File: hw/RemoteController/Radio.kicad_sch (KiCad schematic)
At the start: 89 parts, among them J4 BWSMA-KWE-Z3.5*4.2, U1 LM358, U10 H3-TCD-12-222X+, U12 MAX1473EUI+, U16 H3-TCD-12-222X+, U17 AD8313xRM, U18 LM358, U3 SPF5043Z, U5 XA17-G4K, U6 MAX7044AKA, U8 AD8313xRM, U9 GVA-63, Y2 6.6128 MHz, Y3 10.7 MHz, Y4 13.56 MHz

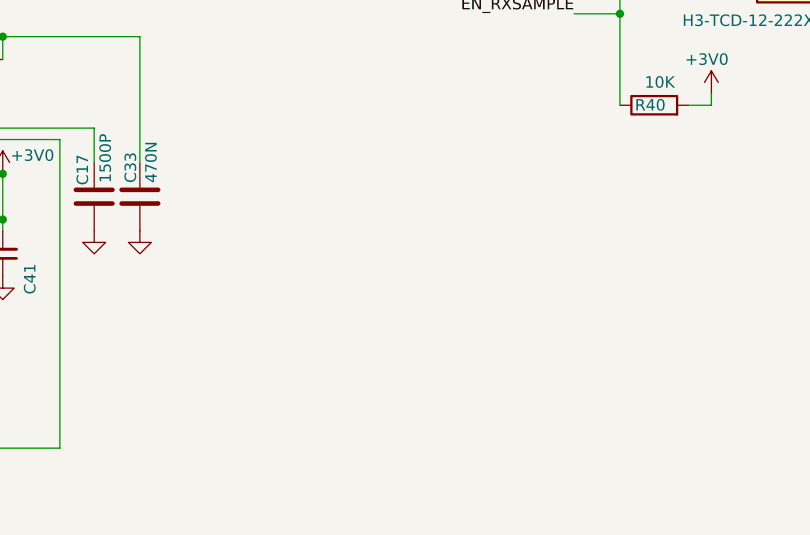
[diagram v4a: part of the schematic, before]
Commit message: remote_ctrl: half way to placement, replace max1473 wit, micrf220
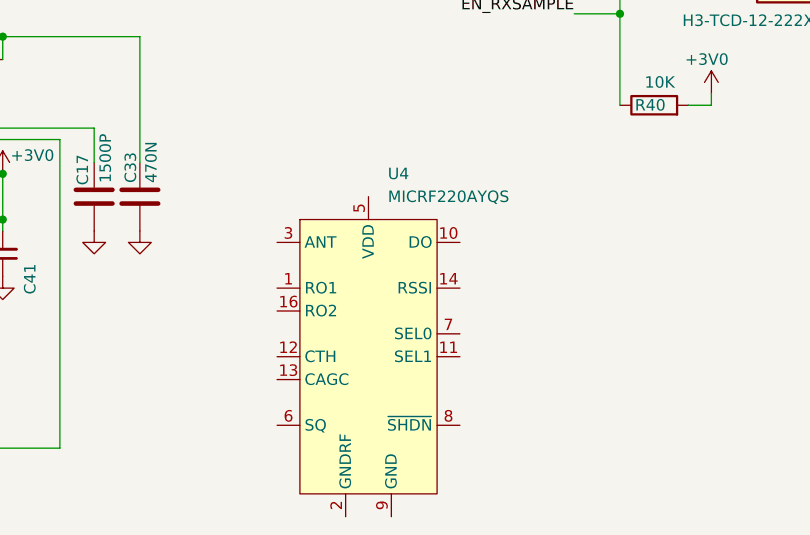
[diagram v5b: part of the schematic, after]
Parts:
- added U4: MICRF220AYQS, Package_SO:QSOP-16_3.9x4.9mm_P0.635mm, symbol RF:MICRF220AYQS
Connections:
- net at U16.4 (OUT): now also C29.2
- new net: U4.2 (GNDRF), U4.4 (GNDRF)
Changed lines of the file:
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@@
+	)
+	(symbol
+		(lib_id "RF:MICRF220AYQS")
+		(at 133.35 177.8 0)
+		(unit 1)
+		(body_style 1)
+		(exclude_from_sim no)
+		(in_bom yes)
+		(on_board yes)
+		(in_pos_files yes)
+		(dnp no)
+		(fields_autoplaced yes)
+		(property "Reference" "U4"
+			(at 135.4933 157.48 0)
+			(show_name no)
+			(do_not_autoplace no)
+			(effects
+				(font
+					(size 1.27 1.27)
+				)
+				(justify left)
+			)
+		)
+		(property "Value" "MICRF220AYQS"
+			(at 135.4933 160.02 0)
+			(show_name no)
+			(do_not_autoplace no)
+			(effects
+				(font
+					(size 1.27 1.27)
+				)
+				(justify left)
+			)
+		)
+		(property "Footprint" "Package_SO:QSOP-16_3.9x4.9mm_P0.635mm"
+			(at 133.35 198.12 0)
+			(hide yes)
+			(show_name no)
+			(do_not_autoplace no)
+			(effects
+				(font
+					(size 1.27 1.27)
+				)
+			)
+		)
+		(property "Datasheet" "http://ww1.microchip.com/downloads/en/DeviceDoc/micrf220.pdf"
+			(at 142.24 158.75 0)
+			(hide yes)
+			(show_name no)
+			(do_not_autoplace no)
+			(effects
+				(font
+					(size 1.27 1.27)
+				)
+			)
+		)
+		(property "Description" "ASK Receiver 3.0-3.6V, 300-450MHz, -110dBm, QSOP-16"
+			(at 133.35 177.8 0)
+			(hide yes)
+			(show_name no)
+			(do_not_autoplace no)
+			(effects
+				(font
+					(size 1.27 1.27)
+				)
+			)
+		)
+		(pin "8"
+		)
+		(pin "6"
+		)
+		(pin "14"
+		)
+		(pin "5"
+		)
+		(pin "1"
+		)
+		(pin "7"
+		)
+		(pin "2"
+		)
+		(pin "12"
+		)
+		(pin "13"
+		)
+		(pin "4"
+		)
+		(pin "3"
+		)
+		(pin "16"
+		)
+		(pin "15"
+		)
+		(pin "9"
+		)
+		(pin "10"
+		)
+		(pin "11"
+		)
+		(instances
+			(project "RemoteController"
+				(path "/2496396e-da71-4b2e-9ac4-452e5130442d/d59aad70-30f5-48a2-8092-bdb11e43ed29"
+					(reference "U4")
+					(unit 1)
+				)
+			)
+		)
 	)
 	(symbol

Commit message: remote_ctrl: continue placemen
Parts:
- removed C25: 470P, Capacitor_SMD:C_0402_1005Metric_Pad0.74x0.62mm_HandSolder, symbol Device:C_Small
- removed C28, C29, C49: 100P, Capacitor_SMD:C_0402_1005Metric_Pad0.74x0.62mm_HandSolder, symbol Device:C_Small
- removed C33: 470N, Capacitor_SMD:C_0402_1005Metric_Pad0.74x0.62mm_HandSolder, symbol Device:C
- removed C40: 10N, Capacitor_SMD:C_0402_1005Metric_Pad0.74x0.62mm_HandSolder, symbol Device:C_Small
- removed C41: 220P, Capacitor_SMD:C_0402_1005Metric_Pad0.74x0.62mm_HandSolder, symbol Device:C_Small
- removed C42: 220P, Capacitor_SMD:C_0402_1005Metric_Pad0.74x0.62mm_HandSolder, symbol Device:C
- removed C50: 2P7, Capacitor_SMD:C_0402_1005Metric_Pad0.74x0.62mm_HandSolder, symbol Device:C_Small
- removed L5: 56N, Inductor_SMD:L_0603_1608Metric_Pad1.05x0.95mm_HandSolder, symbol Device:L
- removed L6, L7: 15N, Inductor_SMD:L_0603_1608Metric_Pad1.05x0.95mm_HandSolder, symbol Device:L
- removed R20: 5K1, Resistor_SMD:R_0402_1005Metric_Pad0.72x0.64mm_HandSolder, symbol Device:R
- removed R21, R22, R23, R24: 0R, Resistor_SMD:R_0402_1005Metric_Pad0.72x0.64mm_HandSolder, symbol Device:R
- removed U12: MAX1473EUI+, Package_SO:TSSOP-28_4.4x9.7mm_P0.65mm, symbol steew:MAX1473EUI+
- removed Y2: 6.6128 MHz, Crystal:Crystal_SMD_HC49-SD, symbol Device:Crystal
- removed Y3: 10.7 MHz, Crystal:Resonator_SMD_Murata_SFECV-3Pin_6.9x2.9mm_HandSoldering, symbol Device:Resonator
- added C25: 10P, Capacitor_SMD:C_0402_1005Metric_Pad0.74x0.62mm_HandSolder, symbol Device:C
- added C33: 100N, Capacitor_SMD:C_0402_1005Metric_Pad0.74x0.62mm_HandSolder, symbol Device:C_Small
- added L5: VHF160808H39NJT, Inductor_SMD:L_0603_1608Metric_Pad1.05x0.95mm_HandSolder, symbol Device:L_Ferrite_Small
- added R41: 100R, Resistor_SMD:R_0402_1005Metric_Pad0.72x0.64mm_HandSolder, symbol Device:R
- added Y2: L327S13CU11L, Crystal:Crystal_SMD_3225-4Pin_3.2x2.5mm_HandSoldering, symbol Device:Crystal_GND24_Small
- C1, C2: value C -> 10P
- C17: value 1500P -> 10P; KiLib_Generator (none) -> SMD_2terminal_chip_molded
- C35: value 10N -> 1000P; KiLib_Generator (none) -> SMD_2terminal_chip_molded
- C38: value 10N -> 100N; KiLib_Generator (none) -> SMD_2terminal_chip_molded
- C39: value 100N -> 4U7
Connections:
- net +3V0: now also C38.1, U4.5 (VDD); no longer C35.2, C38.2, C39.2
- net DATAOUT: now also U4.10 (DO)
- net GND: now also C17.1, C38.2, C39.2, U4.2 (GNDRF), U4.4 (GNDRF), U4.9 (GND), C25.1, C33.2, L5.1, Y2.2 (G), Y2.4 (G); no longer C17.2, C35.1, C38.1, C39.1
- net at U16.4 (OUT): now also C35.2
- net at U4.1 (RO1): now also C25.2, Y2.3
- net RX_BW_SEL1: now reaches U4.11 (SEL1)
- net at U4.12 (CTH): now also C33.1
- net at U4.13 (CAGC): now also C39.1
- net RX_RSSI: now reaches U4.14 (RSSI)
- net at U4.16 (RO2): now also C17.2, Y2.1
- net at U4.3 (ANT): now also C35.1, L5.2
- net RX_SQUELCH: now reaches U4.6 (SQ)
- net RX_BW_SEL0: now reaches U4.7 (SEL0)
- net at U4.8 (~{SHDN}): now also R41.2
- net RXEN renamed RF_SEL0
- net ~{TXEN} renamed RF_SEL1
- new net ~{RX_SHDN}: R41.1
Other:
- note added: "RECEIVER"
- moved on the sheet: U4

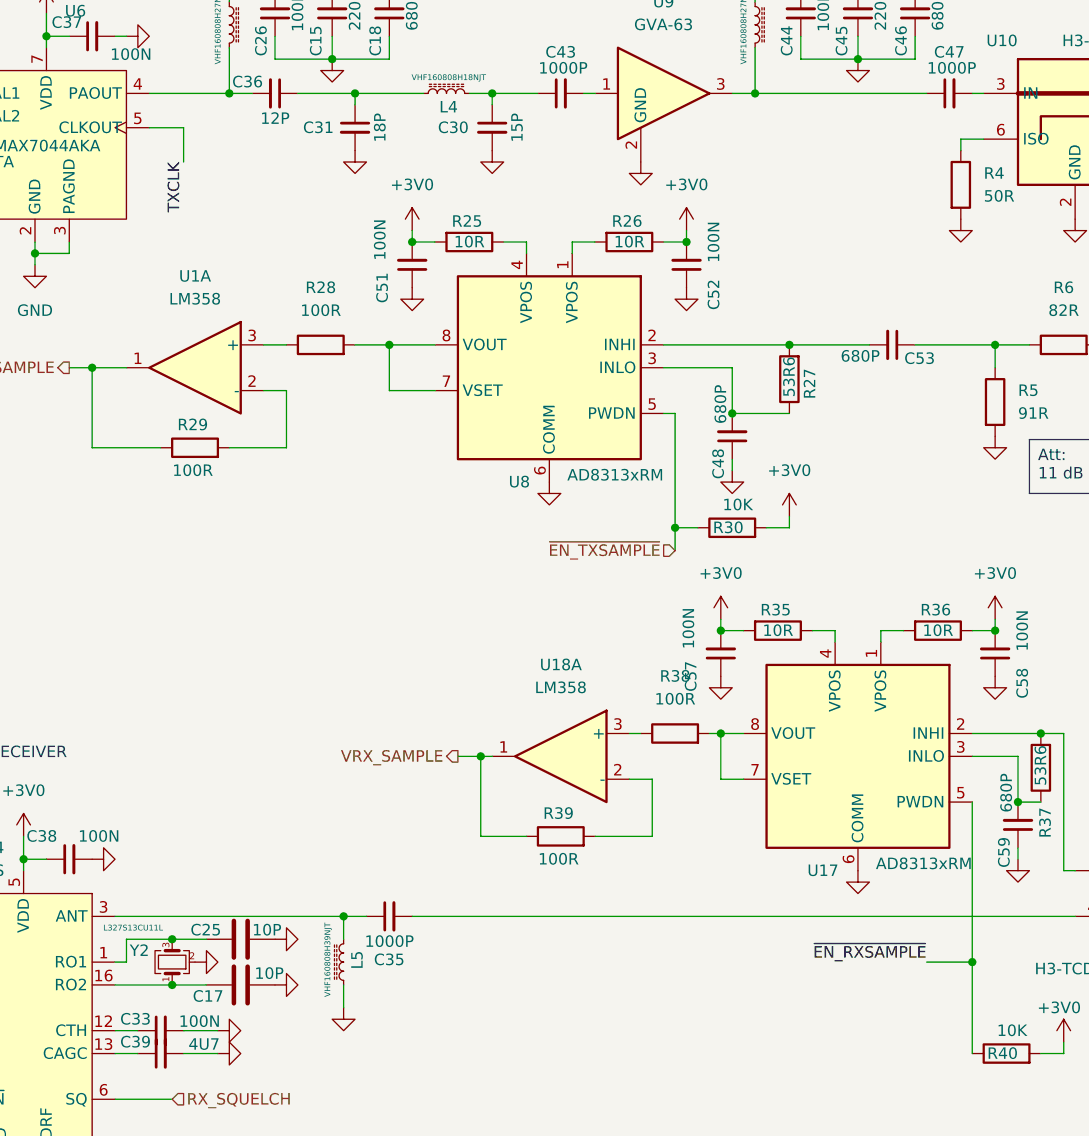
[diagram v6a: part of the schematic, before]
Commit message: remote_ctrl: fix some schematic issues, add battery PTC
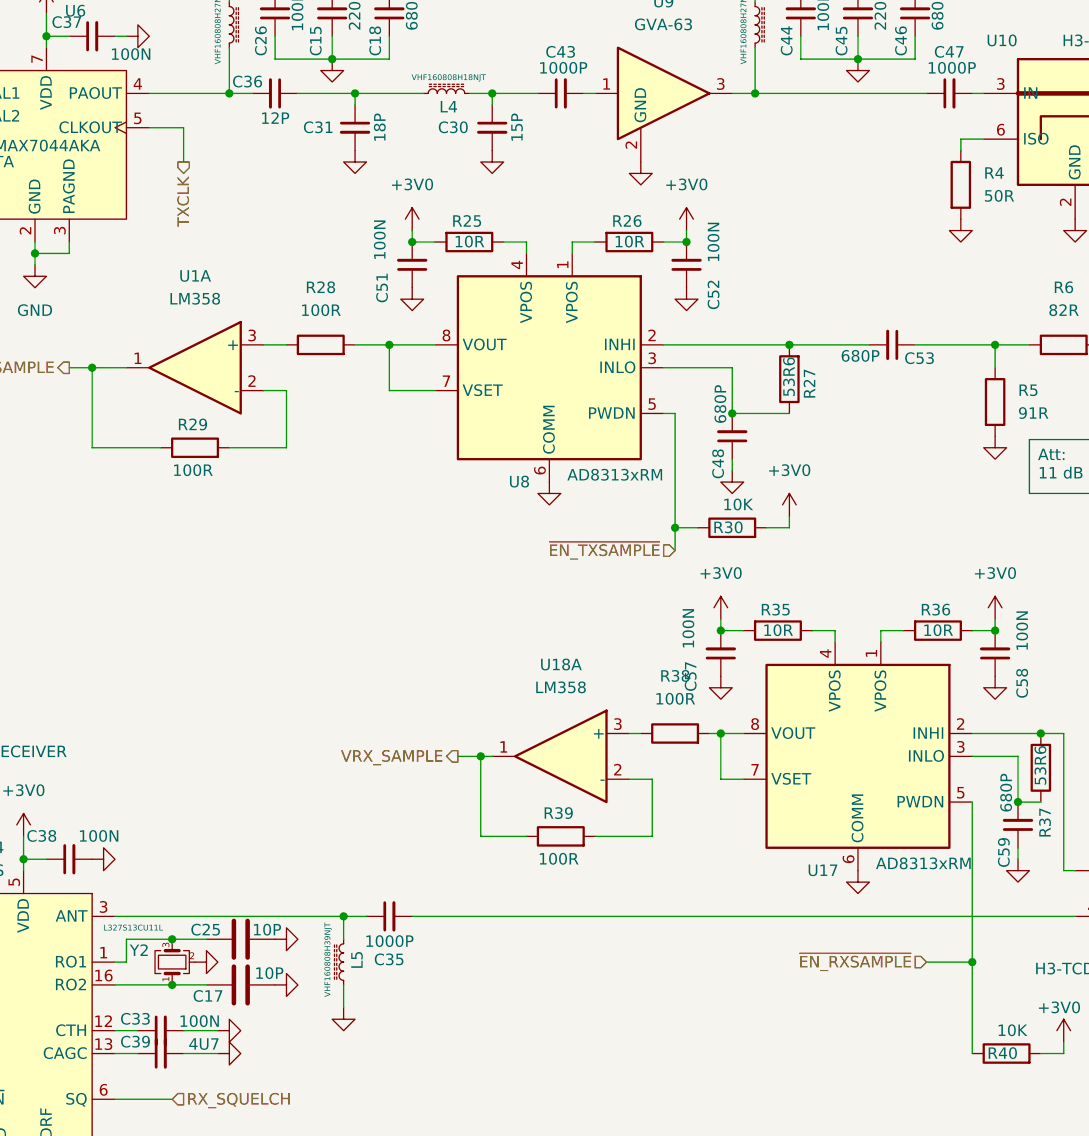
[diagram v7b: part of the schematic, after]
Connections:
- net at U16.4 (OUT): now also C35.2
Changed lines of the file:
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@@
-		)
-	)
-	(label "TXCLK"
-		(at 73.66 50.8 270)
-		(effects
-			(font
-				(size 1.27 1.27)
-			)
-			(justify right bottom)
-		)
-	)
-	(label "~{EN_RXSAMPLE}"
-		(at 156.21 139.7 180)
-		(effects
-			(font
-				(size 1.27 1.27)
-			)
-			(justify right bottom)
 		)
 	)
@@
 		)
 	)
+	(hierarchical_label "TXCLK"
+		(shape output)
+		(at 73.66 50.8 270)
+		(effects
+			(font
+				(size 1.27 1.27)
+			)
+			(justify right)
+		)
+	)
 	(hierarchical_label "RX_BW_SEL1"
 		(shape input)
@@
 		(effects
 			(font
+				(size 1.27 1.27)
+			)
+			(justify right)
+		)
+	)
+	(hierarchical_label "~{EN_RXSAMPLE}"
+		(shape input)
+		(at 156.21 139.7 180)
+		(effects
+			(font

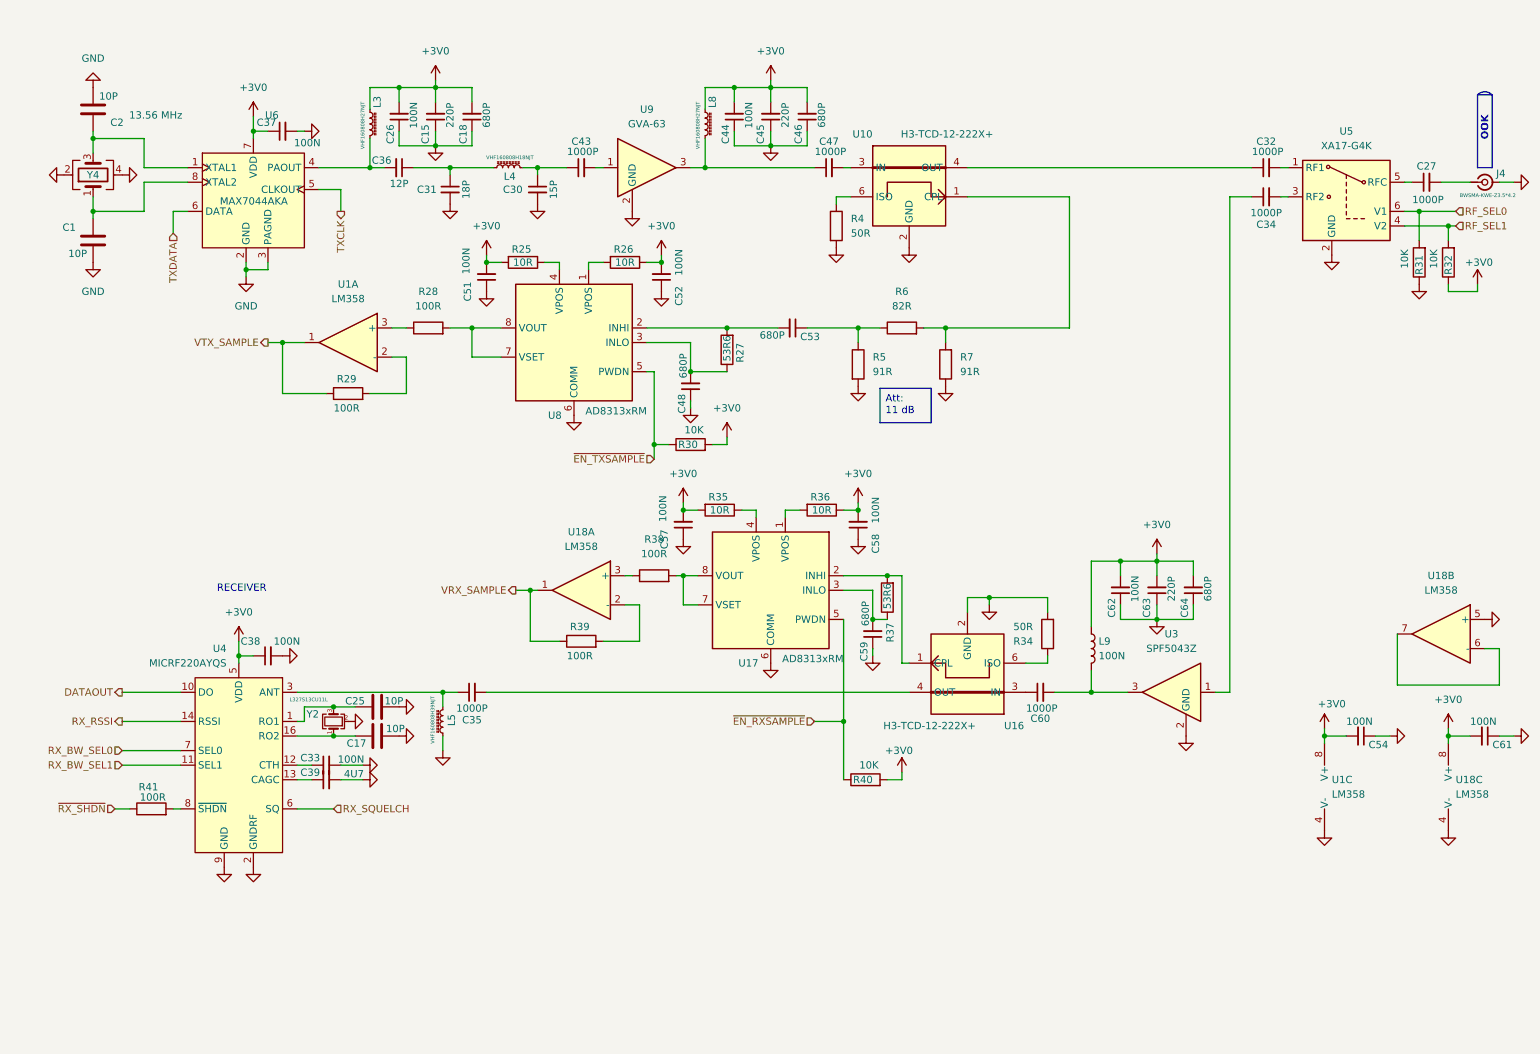
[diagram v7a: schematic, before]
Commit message: remote_ctrl: change logdet to AD8314 and battery holder to SMD
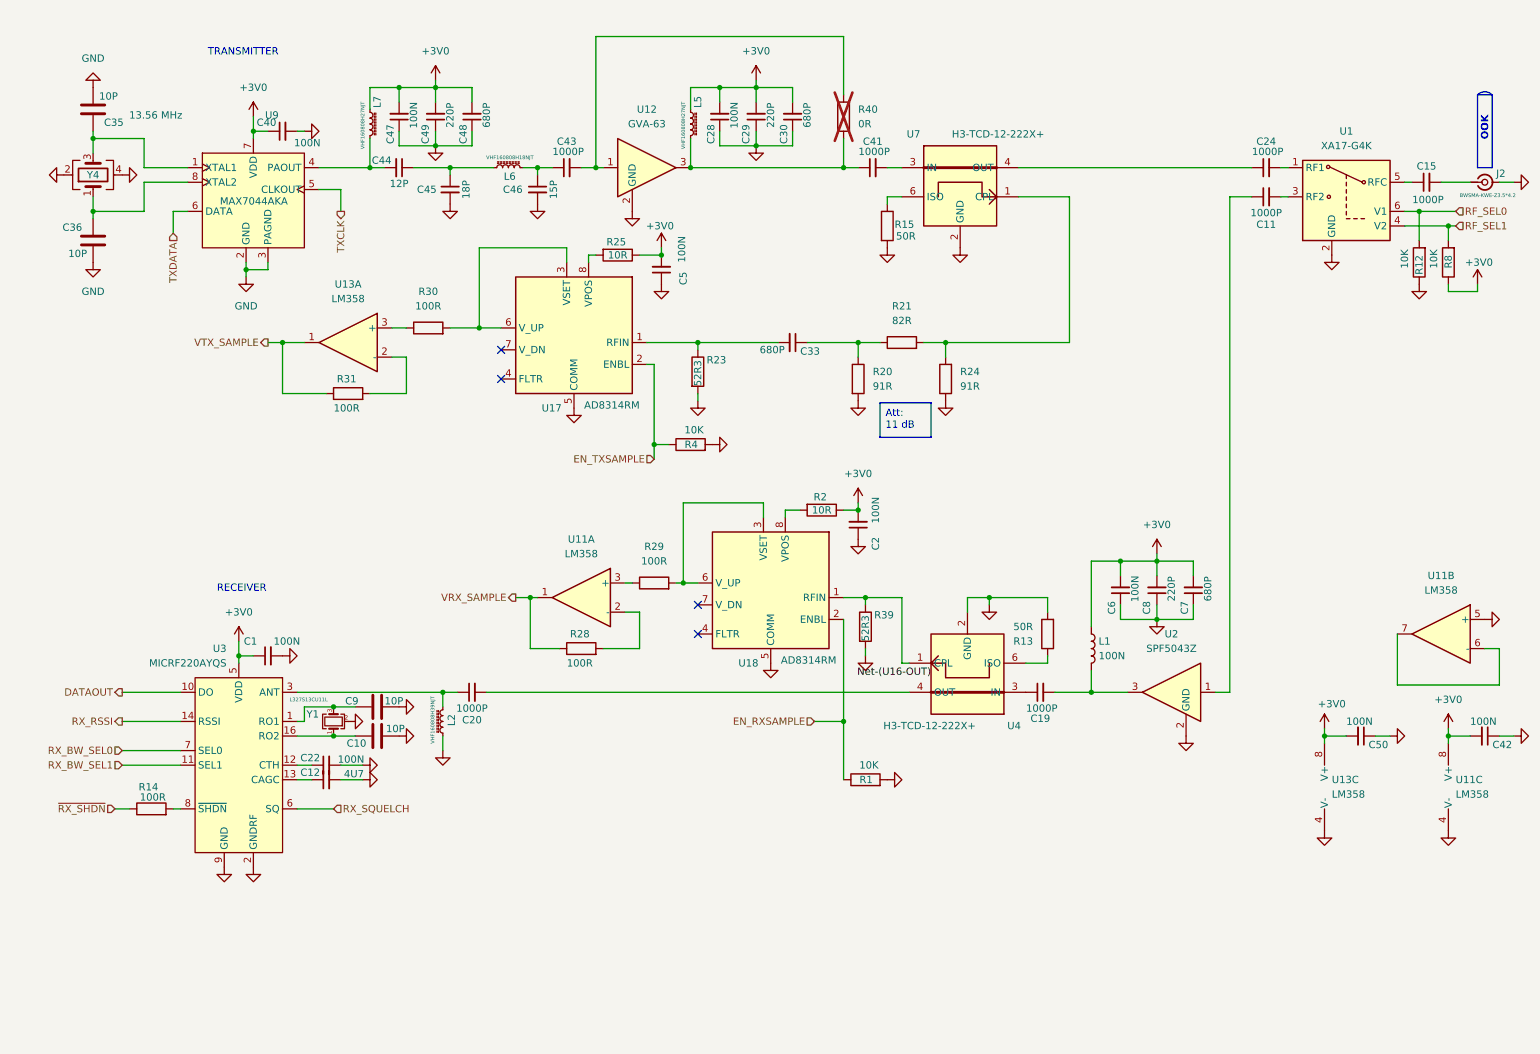
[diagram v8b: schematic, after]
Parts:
- removed C48, C59: 680P, Capacitor_SMD:C_0402_1005Metric_Pad0.74x0.62mm_HandSolder, symbol Device:C_Small
- removed C51, C52, C57: 100N, Capacitor_SMD:C_0402_1005Metric_Pad0.74x0.62mm_HandSolder, symbol Device:C_Small
- removed R26, R35: 10R, Resistor_SMD:R_0402_1005Metric_Pad0.72x0.64mm_HandSolder, symbol Device:R
- removed R27, R37: 53R6, Resistor_SMD:R_0402_1005Metric_Pad0.72x0.64mm_HandSolder, symbol Device:R
- removed U17, U8: AD8313xRM, Package_SO:MSOP-8_3x3mm_P0.65mm, symbol RF_Amplifier:AD8313xRM
- added C5: 100N, Capacitor_SMD:C_0402_1005Metric_Pad0.74x0.62mm_HandSolder, symbol Device:C_Small
- added R23, R39: 52R3, Resistor_SMD:R_0402_1005Metric_Pad0.72x0.64mm_HandSolder, symbol Device:R
- added R40: 0R, Resistor_SMD:R_0402_1005Metric_Pad0.72x0.64mm_HandSolder, symbol Device:R
- added U17, U18: AD8314RM, Package_SO:MSOP-8_3x3mm_P0.65mm, symbol steew:AD8314RM
- C12: renamed from C39; KiLib_Generator (none) -> SMD_2terminal_chip_molded
- C22: renamed from C33; KiLib_Generator (none) -> SMD_2terminal_chip_molded
- L1: renamed from L9; KiLib_Generator (none) -> SMD_2terminal_chip_molded
- U11: renamed from U18; KiLib_Generator (none) -> package/gullwing
- U13: renamed from U1; KiLib_Generator (none) -> package/gullwing
- U2: renamed from U3; KiLib_Generator (none) -> package/gullwing
- U3: renamed from U4; KiLib_Generator (none) -> package/gullwing
- Y1: renamed from Y2; KiLib_Generator (none) -> crystal_resonator_oscillator; private KLC_S4.1 -> (none)
- renumbered C38 to C1, C17 to C10, C34 to C11, C27 to C15, C60 to C19, C58 to C2, C35 to C20, C32 to C24, C44 to C28, C45 to C29, C46 to C30, C53 to C33, C2 to C35, C1 to C36, C37 to C40, C47 to C41, C61 to C42, C36 to C44, C31 to C45, C30 to C46, C26 to C47, C18 to C48, C15 to C49, C54 to C50, C62 to C6, C64 to C7, C63 to C8, C25 to C9, J4 to J2, L5 to L2, L8 to L5, L4 to L6, L3 to L7, R40 to R1, R31 to R12, R34 to R13, R41 to R14, R4 to R15, R36 to R2, R5 to R20, R6 to R21, R7 to R24, R39 to R28, R38 to R29, R28 to R30, R29 to R31, R30 to R4, R32 to R8, U5 to U1, U9 to U12, U16 to U4, U10 to U7, U6 to U9
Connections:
- net +3V0: now also R25.1, C5.2; no longer R1.2, R25.2, R4.2
- net GND: now also R1.2, R4.2, C5.1, R23.2, R39.2, U17.5 (COMM), U18.5 (COMM)
- net at R2.2: now also U18.8 (VPOS)
- net at U4.1 (CPL): now also R39.1, U18.1 (RFIN)
- net at R29.2: now also U18.3 (VSET), U18.6 (V_UP)
- net at C41.1, L5.2, U12.3: now also R40.1
- net Net-(U16-OUT): now reaches U4.4 (OUT)
- net at C33.2: now also R23.1, U17.1 (RFIN)
- net at R30.2: now also U17.3 (VSET), U17.6 (V_UP)
- net at C43.2, U12.1: now also R40.2
- net ~{EN_RXSAMPLE} renamed EN_RXSAMPLE
- net EN_RXSAMPLE: now also U18.2 (ENBL)
- net ~{EN_TXSAMPLE} renamed EN_TXSAMPLE
- net EN_TXSAMPLE: now also U17.2 (ENBL)
- new net: R25.2, U17.8 (VPOS)
- no-connect marks 0 -> 4
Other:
- note added: "TRANSMITTER"
- moved on the sheet: C28, C29, C30, C33, C41, C43, L5, R15, R20, R21, R24, R25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
